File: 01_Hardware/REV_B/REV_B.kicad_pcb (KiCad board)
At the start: 2 copper layers, 65 x 30 mm, 65 parts, among them J1 RaspberryPi, J10 Conn_01x03, J11 Conn_01x03, J13 Conn_01x03, J14 Conn_01x03, J15 Conn_01x03, J16 Conn_01x08_Male, J2 Conn_01x02, J3 Conn_01x02, J4 Conn_01x02, J5 Conn_01x08_Male, J6 Conn_01x03, J7 Conn_01x03, J8 Conn_01x03, J9 Conn_01x03, U1 TB6612FNG, U2 MCP3008, U3 PCA9685PW, U5 BSS138PS, U6 BSS138PS, U7 BSS138PS, U8 BSS138PS

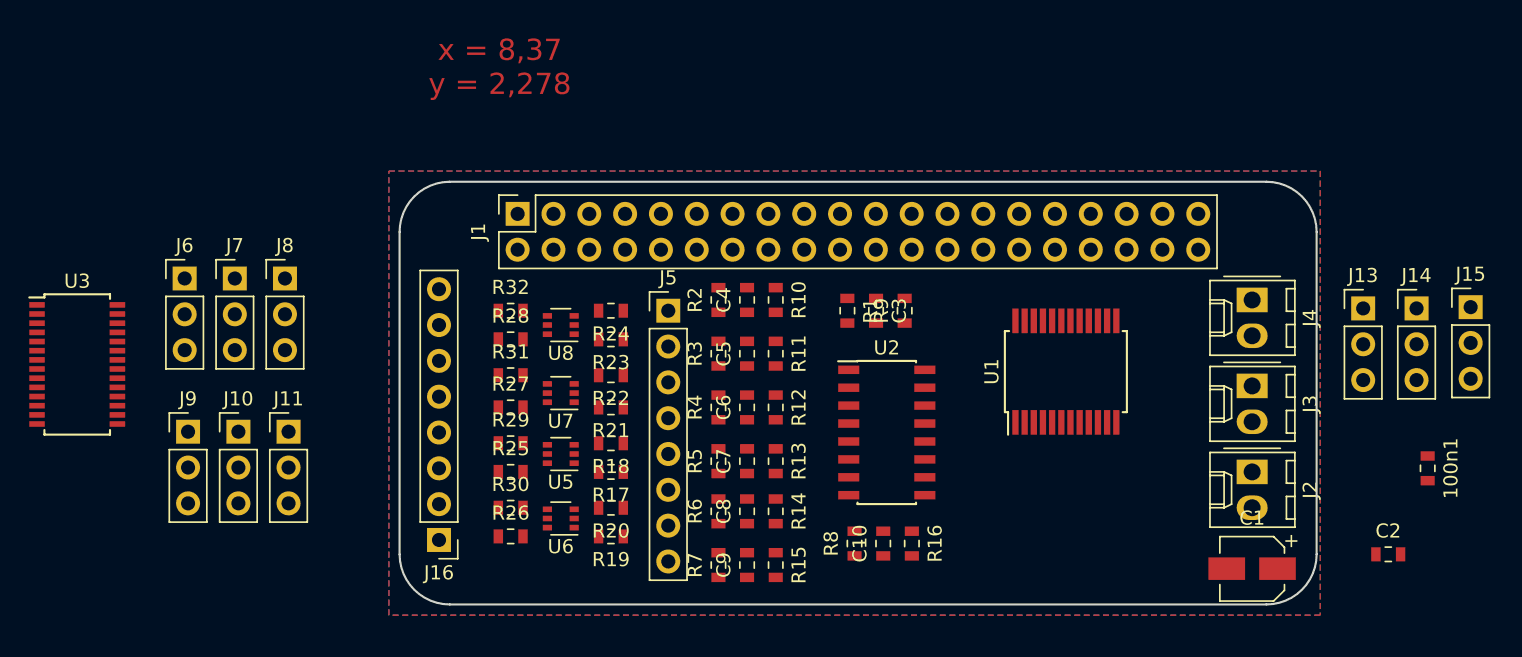
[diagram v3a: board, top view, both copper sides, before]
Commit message: kicad version  REVB added
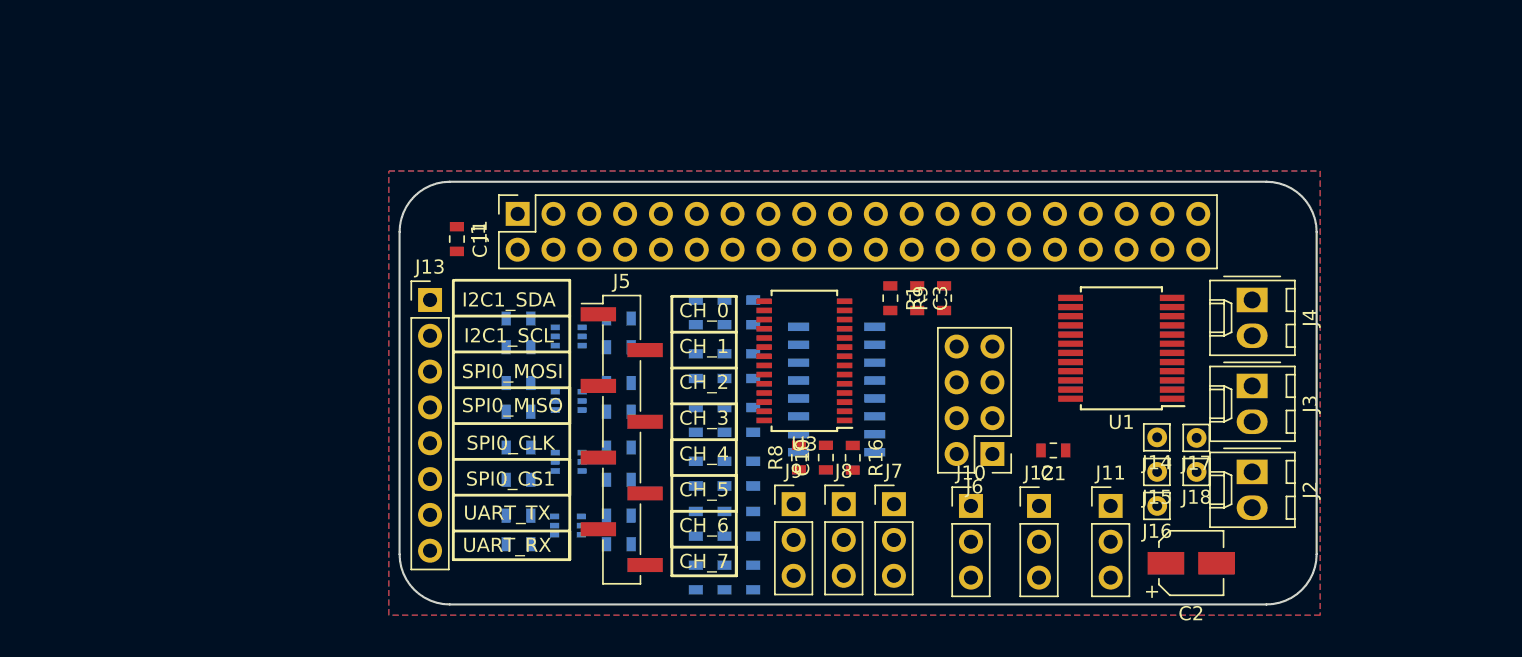
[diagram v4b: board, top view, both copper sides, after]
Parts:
- removed 100n1: C, Capacitor_SMD:C_0603_1608Metric
- removed U8: BSS138PS, Package_TO_SOT_SMD:SOT-363_SC-70-6
- added C11: 10n, Capacitor_SMD:C_0603_1608Metric, F.Cu at (4.06, 4.06)
- added J12: Conn_01x03, Connector_PinHeader_2.54mm:PinHeader_1x03_P2.54mm_Vertical, F.Cu at (45.3, 23.0)
- added J17: Conn_01x01, Connector_Pin:Pin_D0.7mm_L6.5mm_W1.8mm_FlatFork, F.Cu at (56.5, 18.2)
- added J18: Conn_01x01, Connector_Pin:Pin_D0.7mm_L6.5mm_W1.8mm_FlatFork, F.Cu at (56.5, 20.6)
- added U4: BSS138PS, Package_TO_SOT_SMD:SOT-363_SC-70-6, B.Cu at (11.9, 24.4)
- C1: value 10u -> 100n; footprint Capacitor_SMD:CP_Elec_4x4.5 -> Capacitor_SMD:C_0603_1608Metric
- C2: value 100n -> 10u; footprint Capacitor_SMD:C_0603_1608Metric -> Capacitor_SMD:CP_Elec_4x4.5
- C3: value 10n -> 100n
- C4, C5, C6, C7, C8, C9, R10, R11, R12, R13, R14, R15, R17, R18, R19, R2, R20, R21, R22, R23, R24, R25, R26, R27, R28, R29, R3, R30, R31, R32, R4, R5, R6, R7, U2, U5, U6, U7: moved to B.Cu
- J13: value Conn_01x03 -> Conn_01x08_Male; footprint Connector_PinHeader_2.54mm:PinHeader_1x03_P2.54mm_Vertical -> Connector_PinHeader_2.54mm:PinHeader_1x08_P2.54mm_Vertical
- J14, J15: value Conn_01x03 -> Conn_01x01; footprint Connector_PinHeader_2.54mm:PinHeader_1x03_P2.54mm_Vertical -> Connector_Pin:Pin_D0.7mm_L6.5mm_W1.8mm_FlatFork
- J16: value Conn_01x08_Male -> Conn_01x01; footprint Connector_PinHeader_2.54mm:PinHeader_1x08_P2.54mm_Vertical -> Connector_Pin:Pin_D0.7mm_L6.5mm_W1.8mm_FlatFork
- J5: footprint Connector_PinHeader_2.54mm:PinHeader_1x08_P2.54mm_Vertical -> Connector_PinHeader_2.54mm:PinHeader_1x08_P2.54mm_Vertical_SMD_Pin1Left
- J6: value Conn_01x03 -> Conn_02x04_Counter_Clockwise; footprint Connector_PinHeader_2.54mm:PinHeader_1x03_P2.54mm_Vertical -> Connector_PinHeader_2.54mm:PinHeader_2x04_P2.54mm_Vertical
- moved J13 66.2 mm to (2.16, 8.38)
- moved J6 58.6 mm to (42.0, 19.3), turned to 180 degrees
- moved J11 58.5 mm to (50.4, 23.0)
- moved J10 52.2 mm to (40.5, 23.0)
- moved U3 51.6 mm to (28.7, 12.7), turned to 180 degrees
- moved J16 51.0 mm to (53.7, 23.0), turned to 0 degrees
- moved J7 49.4 mm to (35.1, 22.9)
- moved J9 43.2 mm to (27.9, 22.9)
- moved J8 42.7 mm to (31.5, 22.9)
- moved J15 25.1 mm to (53.7, 20.6)
- moved J14 20.5 mm to (53.7, 18.1)
- moved R24 16.6 mm to (15.5, 25.7)
- moved R32 16.6 mm to (8.43, 25.7)
- moved C1 16.4 mm to (46.4, 19.1)
- moved R19 15.5 mm to (15.5, 9.70)
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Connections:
- C1 pad 1: +BATT -> +3V3
- C3 pad 1: Net-(C3-Pad1) -> +BATT
- J1 pad 10: (no net) -> UART_RX_LV
- J1 pad 19: Net-(J1-Pad19) -> SPI0_MOSI_LV
- J1 pad 21: Net-(J1-Pad21) -> SPI0_MISO_LV
- J1 pad 23: Net-(J1-Pad23) -> SPI0_CLK_LV
- J1 pad 26: (no net) -> SPI0_CS1_LV
- J1 pad 3: (no net) -> I2C1_SDA_LV
- J1 pad 38: (no net) -> Net-(J1-Pad38)
- J1 pad 5: (no net) -> I2C1_SCL_LV
- J1 pad 8: (no net) -> UART_TX_LV
- J10 pad 1: Net-(J10-Pad1) -> +5V
- J10 pad 3: GND -> +5V
- J11 pad 1: Net-(J11-Pad1) -> +3V3
- J11 pad 2: +5V -> +3V3
- J11 pad 3: GND -> +3V3
- J13 pad 1: +5V -> I2C1_SDA_HV
- J13 pad 2: +5V -> I2C1_SCL_HV
- J13 pad 3: +5V -> Net-(J13-Pad3)
- J14 pad 1: +3V3 -> Net-(J14-Pad1)
- J15 pad 1: GND -> Net-(J15-Pad1)
- J7 pad 2: Net-(J7-Pad2) -> +5V
- J7 pad 3: Net-(J7-Pad3) -> GND
- J8 pad 2: Net-(J8-Pad2) -> +5V
- J8 pad 3: Net-(J8-Pad3) -> GND
- R1 pad 1: Net-(C3-Pad1) -> Net-(C4-Pad1)
- R10 pad 2: Net-(C4-Pad1) -> Net-(C5-Pad1)
- R11 pad 2: Net-(C5-Pad1) -> Net-(C6-Pad1)
- R12 pad 2: Net-(C6-Pad1) -> Net-(C7-Pad1)
- R13 pad 2: Net-(C7-Pad1) -> Net-(C8-Pad1)
- R14 pad 2: Net-(C8-Pad1) -> Net-(C9-Pad1)
- R15 pad 2: Net-(C9-Pad1) -> Net-(C10-Pad1)
- R16 pad 2: Net-(C10-Pad1) -> Net-(C11-Pad1)
- R17 pad 2: Net-(R17-Pad2) -> SPI0_MOSI_LV
- R18 pad 2: Net-(R18-Pad2) -> SPI0_MISO_LV
- R19 pad 2: Net-(R19-Pad2) -> I2C1_SDA_LV
- R2 pad 1: Net-(C4-Pad1) -> Net-(C5-Pad1)
- R20 pad 2: Net-(R20-Pad2) -> I2C1_SCL_LV
- R21 pad 2: Net-(R21-Pad2) -> SPI0_CLK_LV
- R22 pad 2: Net-(R22-Pad2) -> SPI0_CS1_LV
- R23 pad 2: Net-(R23-Pad2) -> UART_TX_LV
- R24 pad 2: Net-(R24-Pad2) -> UART_RX_LV
- R25 pad 2: Net-(J16-Pad3) -> Net-(J13-Pad3)
- R26 pad 2: Net-(J16-Pad1) -> I2C1_SDA_HV
- R27 pad 2: Net-(J16-Pad5) -> Net-(J13-Pad5)
- R28 pad 2: Net-(J16-Pad7) -> Net-(J13-Pad7)
- R29 pad 2: Net-(J16-Pad4) -> Net-(J13-Pad4)
- R3 pad 1: Net-(C5-Pad1) -> Net-(C6-Pad1)
- R30 pad 2: Net-(J16-Pad2) -> I2C1_SCL_HV
- R31 pad 2: Net-(J16-Pad6) -> Net-(J13-Pad6)
- R32 pad 2: Net-(J16-Pad8) -> Net-(J13-Pad8)
- R4 pad 1: Net-(C6-Pad1) -> Net-(C7-Pad1)
- R5 pad 1: Net-(C7-Pad1) -> Net-(C8-Pad1)
- R6 pad 1: Net-(C8-Pad1) -> Net-(C9-Pad1)
- R7 pad 1: Net-(C9-Pad1) -> Net-(C10-Pad1)
- R8 pad 1: Net-(C10-Pad1) -> Net-(C11-Pad1)
- R9 pad 2: Net-(C3-Pad1) -> Net-(C4-Pad1)
- U1 pad 16: (no net) -> Net-(J1-Pad38)
- U2 pad 1: Net-(C3-Pad1) -> Net-(C4-Pad1)
- U2 pad 11: Net-(J1-Pad19) -> SPI0_MOSI_LV
- U2 pad 12: Net-(J1-Pad21) -> SPI0_MISO_LV
- U2 pad 13: Net-(J1-Pad23) -> SPI0_CLK_LV
- U2 pad 2: Net-(C4-Pad1) -> Net-(C5-Pad1)
- U2 pad 3: Net-(C5-Pad1) -> Net-(C6-Pad1)
- U2 pad 4: Net-(C6-Pad1) -> Net-(C7-Pad1)
- U2 pad 5: Net-(C7-Pad1) -> Net-(C8-Pad1)
- U2 pad 6: Net-(C8-Pad1) -> Net-(C9-Pad1)
- U2 pad 7: Net-(C9-Pad1) -> Net-(C10-Pad1)
- U2 pad 8: Net-(C10-Pad1) -> Net-(C11-Pad1)
- U3 pad 10: Net-(J7-Pad2) -> Net-(J6-Pad5)
- U3 pad 11: Net-(J7-Pad3) -> Net-(J6-Pad6)
- U3 pad 12: Net-(J8-Pad1) -> Net-(J6-Pad7)
- U3 pad 13: Net-(J8-Pad2) -> Net-(J6-Pad8)
- U3 pad 15: Net-(J8-Pad3) -> Net-(J9-Pad1)
- U3 pad 16: (no net) -> Net-(J8-Pad1)
- U3 pad 17: (no net) -> Net-(J7-Pad1)
- U3 pad 18: (no net) -> Net-(J18-Pad1)
- U3 pad 19: Net-(J9-Pad1) -> Net-(J17-Pad1)
- U3 pad 20: Net-(J10-Pad1) -> Net-(J16-Pad1)
- U3 pad 21: Net-(J11-Pad1) -> Net-(J15-Pad1)
- U3 pad 22: (no net) -> Net-(J14-Pad1)
- U3 pad 26: (no net) -> I2C1_SCL_HV
- U3 pad 27: (no net) -> I2C1_SDA_HV
- U3 pad 9: Net-(J7-Pad1) -> Net-(J6-Pad4)
- U5 pad 1: Net-(R17-Pad2) -> I2C1_SDA_LV
- U5 pad 3: Net-(J16-Pad4) -> I2C1_SCL_HV
- U5 pad 4: Net-(R18-Pad2) -> I2C1_SCL_LV
- U5 pad 6: Net-(J16-Pad3) -> I2C1_SDA_HV
- U6 pad 1: Net-(R19-Pad2) -> SPI0_CLK_LV
- U6 pad 3: Net-(J16-Pad2) -> Net-(J13-Pad6)
- U6 pad 4: Net-(R20-Pad2) -> SPI0_CS1_LV
- U6 pad 6: Net-(J16-Pad1) -> Net-(J13-Pad5)
- U7 pad 1: Net-(R21-Pad2) -> UART_TX_LV
- U7 pad 3: Net-(J16-Pad6) -> Net-(J13-Pad8)
- U7 pad 4: Net-(R22-Pad2) -> UART_RX_LV
- U7 pad 6: Net-(J16-Pad5) -> Net-(J13-Pad7)
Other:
- board text added: "CH_0"
- board text added: "CH_1"
- board text added: "CH_2"
- board text added: "CH_3"
- board text added: "CH_4"
- board text added: "CH_5"
- board text added: "CH_6"
- board text added: "CH_7"
- board text added: "I2C1_SCL"
- board text added: "I2C1_SDA"
- board text added: "SPI0_CLK"
- board text added: "SPI0_CS1"
- board text added: "SPI0_MISO"
- board text added: "SPI0_MOSI"
- board text added: "UART_RX"
- board text added: "UART_TX"
- board text removed: "x = 8,37 y = 2,278"

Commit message: Routing started
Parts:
- removed J14, J15, J16, J17, J18: Conn_01x01, Connector_Pin:Pin_D0.7mm_L6.5mm_W1.8mm_FlatFork
- added D1: LED_CRGB, LED_SMD:LED_Avago_PLCC4_3.2x2.8mm_CW, F.Cu at (61.0, 27.1)
- added R33: 10k, Resistor_SMD:R_0603_1608Metric, B.Cu at (6.48, 10.7)
- added R34: 10k, Resistor_SMD:R_0603_1608Metric, B.Cu at (13.7, 19.1)
- added R35: 10k, Resistor_SMD:R_0603_1608Metric, B.Cu at (6.73, 21.3)
- added R36: 10k, Resistor_SMD:R_0603_1608Metric, B.Cu at (13.7, 24.4)
- added R37: 10k, Resistor_SMD:R_0603_1608Metric, B.Cu at (6.60, 26.7)
- added R38: 10k, Resistor_SMD:R_0603_1608Metric, B.Cu at (6.73, 13.6)
- added R39: 10k, Resistor_SMD:R_0603_1608Metric, B.Cu at (6.48, 8.38)
- added R40: 10k, Resistor_SMD:R_0603_1608Metric, B.Cu at (6.73, 18.8)
- added R41: 10k, Resistor_SMD:R_0603_1608Metric, B.Cu at (6.73, 24.5)
- added R42: 10k, Resistor_SMD:R_0603_1608Metric, B.Cu at (13.7, 15.7)
- added R43: 10k, Resistor_SMD:R_0603_1608Metric, B.Cu at (13.7, 10.7)
- added R44: 10k, Resistor_SMD:R_0603_1608Metric, B.Cu at (13.7, 21.3)
- added R45: 10k, Resistor_SMD:R_0603_1608Metric, B.Cu at (13.7, 26.7)
- C10, R16: moved to B.Cu
- C4, R10, U2: moved to F.Cu
- J13, J5: value Conn_01x08_Male -> Conn_01x08
- R13: value 22k -> 1k
- R17: value 10k -> 22k; moved to F.Cu
- R18, R19, R20, R21, R22, R23, R24, R25, R26, R27, R28, R29: value 10k -> 220
- R9: value 1k -> 10k
- moved R18 37.5 mm to (20.2, -20.9)
- moved R19 37.5 mm to (20.2, -27.5)
- moved R20 37.5 mm to (20.2, -25.5)
- moved R22 37.5 mm to (20.2, -16.1)
- moved R23 37.5 mm to (20.2, -13.5)
- moved R24 37.5 mm to (20.2, -11.5)
- moved R25 37.5 mm to (13.1, -22.9)
- moved R26 37.5 mm to (13.1, -27.5)
- moved R27 37.5 mm to (13.1, -18.4)
- moved R28 37.5 mm to (13.1, -13.5)
- moved R29 37.5 mm to (13.1, -20.9)
- moved R21 28.5 mm to (44.1, 18.5), turned to 90 degrees
- moved C11 26.4 mm to (20.9, 24.4), turned to 0 degrees
- moved U3 25.1 mm to (42.0, -8.51)
- moved R32 18.1 mm to (13.7, 8.38), turned to 180 degrees
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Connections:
- R10 pad 1: Net-(J5-Pad2) -> Net-(J5-Pad1)
- R10 pad 2: Net-(C5-Pad1) -> Net-(C4-Pad1)
- R11 pad 1: Net-(J5-Pad3) -> Net-(J5-Pad2)
- R11 pad 2: Net-(C6-Pad1) -> Net-(C5-Pad1)
- R12 pad 1: Net-(J5-Pad4) -> Net-(J5-Pad3)
- R12 pad 2: Net-(C7-Pad1) -> Net-(C6-Pad1)
- R13 pad 1: Net-(J5-Pad5) -> Net-(J5-Pad4)
- R13 pad 2: Net-(C8-Pad1) -> Net-(C7-Pad1)
- R14 pad 1: Net-(J5-Pad6) -> Net-(J5-Pad5)
- R14 pad 2: Net-(C9-Pad1) -> Net-(C8-Pad1)
- R15 pad 1: Net-(J5-Pad7) -> Net-(J5-Pad6)
- R15 pad 2: Net-(C10-Pad1) -> Net-(C9-Pad1)
- R16 pad 1: Net-(J5-Pad8) -> Net-(J5-Pad7)
- R16 pad 2: Net-(C11-Pad1) -> Net-(C10-Pad1)
- R17 pad 1: +3V3 -> Net-(J5-Pad8)
- R17 pad 2: SPI0_MOSI_LV -> Net-(C11-Pad1)
- R18 pad 1: +3V3 -> Net-(D1-Pad2)
- R18 pad 2: SPI0_MISO_LV -> Net-(R18-Pad2)
- R19 pad 1: +3V3 -> Net-(D1-Pad3)
- R19 pad 2: I2C1_SDA_LV -> Net-(R19-Pad2)
- R20 pad 1: +3V3 -> Net-(D1-Pad4)
- R20 pad 2: I2C1_SCL_LV -> Net-(R20-Pad2)
- R21 pad 1: +3V3 -> Net-(J6-Pad1)
- R21 pad 2: SPI0_CLK_LV -> Net-(R21-Pad2)
- R22 pad 1: +3V3 -> Net-(J6-Pad2)
- R22 pad 2: SPI0_CS1_LV -> Net-(R22-Pad2)
- R23 pad 1: +3V3 -> Net-(J6-Pad3)
- R23 pad 2: UART_TX_LV -> Net-(R23-Pad2)
- R24 pad 1: +3V3 -> Net-(J6-Pad4)
- R24 pad 2: UART_RX_LV -> Net-(R24-Pad2)
- R25 pad 1: +5V -> Net-(J6-Pad5)
- R25 pad 2: Net-(J13-Pad3) -> Net-(R25-Pad2)
- R26 pad 1: +5V -> Net-(J6-Pad6)
- R26 pad 2: I2C1_SDA_HV -> Net-(R26-Pad2)
- R27 pad 1: +5V -> Net-(J6-Pad7)
- R27 pad 2: Net-(J13-Pad5) -> Net-(R27-Pad2)
- R28 pad 1: +5V -> Net-(J6-Pad8)
- R28 pad 2: Net-(J13-Pad7) -> Net-(R28-Pad2)
- R29 pad 1: +5V -> Net-(J9-Pad1)
- R29 pad 2: Net-(J13-Pad4) -> Net-(R29-Pad2)
- R30 pad 1: +5V -> +3V3
- R30 pad 2: I2C1_SCL_HV -> SPI0_MOSI_LV
- R31 pad 1: +5V -> +3V3
- R31 pad 2: Net-(J13-Pad6) -> SPI0_MISO_LV
- R32 pad 1: +5V -> +3V3
- R32 pad 2: Net-(J13-Pad8) -> I2C1_SDA_LV
- R9 pad 1: Net-(J5-Pad1) -> GND
- R9 pad 2: Net-(C4-Pad1) -> Net-(R9-Pad2)
- U3 pad 10: Net-(J6-Pad5) -> Net-(R25-Pad2)
- U3 pad 11: Net-(J6-Pad6) -> Net-(R26-Pad2)
- U3 pad 12: Net-(J6-Pad7) -> Net-(R27-Pad2)
- U3 pad 13: Net-(J6-Pad8) -> Net-(R28-Pad2)
- U3 pad 15: Net-(J9-Pad1) -> Net-(R29-Pad2)
- U3 pad 18: Net-(J18-Pad1) -> Net-(R20-Pad2)
- U3 pad 19: Net-(J17-Pad1) -> Net-(R19-Pad2)
- U3 pad 20: Net-(J16-Pad1) -> Net-(R18-Pad2)
- U3 pad 21: Net-(J15-Pad1) -> (no net)
- U3 pad 22: Net-(J14-Pad1) -> (no net)
- U3 pad 23: (no net) -> Net-(R9-Pad2)
- U3 pad 6: Net-(J6-Pad1) -> Net-(R21-Pad2)
- U3 pad 7: Net-(J6-Pad2) -> Net-(R22-Pad2)
- U3 pad 8: Net-(J6-Pad3) -> Net-(R23-Pad2)
- U3 pad 9: Net-(J6-Pad4) -> Net-(R24-Pad2)
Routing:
- net +5V: track 0.00 -> 84.8 mm, vias 0 -> 2
- net +3V3: track 0.00 -> 75.4 mm, vias 0 -> 5
- net SPI0_CLK_LV: track 0.00 -> 48.3 mm, vias 0 -> 1
- net SPI0_CS1_LV: track 0.00 -> 45.8 mm, vias 0 -> 1
- net UART_TX_LV: track 0.00 -> 44.9 mm, vias 0 -> 1
- net UART_RX_LV: track 0.00 -> 39.1 mm, vias 0 -> 2
- net Net-(J1-Pad24): track 0.00 -> 21.6 mm
- net SPI0_MISO_LV: track 0.00 -> 21.5 mm
- net SPI0_MOSI_LV: track 0.00 -> 20.6 mm, vias 0 -> 1
- net I2C1_SDA_LV: track 0.00 -> 16.1 mm, vias 0 -> 1
- net Net-(J5-Pad1): track 0.00 -> 15.7 mm
- net Net-(J13-Pad8): track 0.00 -> 14.2 mm
- net I2C1_SCL_LV: track 0.00 -> 13.8 mm, vias 0 -> 1
- net Net-(J13-Pad6): track 0.00 -> 12.4 mm
- net Net-(J13-Pad4): track 0.00 -> 12.3 mm
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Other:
- net class Default: clearance 0.2 -> 0.1524; trace_width 0.25 -> 0.1524; via_dia 0.8 -> 0.6858; via_drill 0.4 -> 0.3302
- rule pad_to_mask_clearance: 0.2 -> 0.0508
- rule trace_clearance: 0.2 -> 0.1524
- rule trace_min: 0.2 -> 0.1524
- rule via_min_drill: 0.3 -> 0.254
- rule via_min_size: 0.4 -> 0.508

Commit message: Routing almost done
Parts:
- C3, U1, U3: moved to B.Cu
- J6: footprint Connector_PinHeader_2.54mm:PinHeader_2x04_P2.54mm_Vertical -> Connector_PinHeader_2.54mm:PinHeader_2x04_P2.54mm_Vertical_SMD
- moved R26 49.0 mm to (36.2, 15.7), turned to 180 degrees
- moved R19 48.3 mm to (27.6, 20.2)
- moved R20 46.9 mm to (31.1, 20.2), turned to 0 degrees
- moved R29 45.1 mm to (24.5, 22.7), turned to 90 degrees
- moved R25 43.5 mm to (36.2, 14.0), turned to 180 degrees
- moved R27 42.7 mm to (36.2, 17.5), turned to 180 degrees
- moved R28 40.1 mm to (36.2, 19.3), turned to 180 degrees
- moved R18 36.8 mm to (24.6, 15.6), turned to 90 degrees
- moved R22 29.4 mm to (36.2, 8.64)
- moved R23 28.8 mm to (36.2, 10.4)
- moved R24 28.6 mm to (36.2, 12.2)
- moved U3 25.4 mm to (29.7, 13.7)
- moved C3 16.7 mm to (57.5, 9.65)
- moved R21 14.1 mm to (36.2, 6.86), turned to 180 degrees
- moved J6 7.37 mm to (35.3, 13.2), turned to 0 degrees
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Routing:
- net Net-(R21-Pad2): track 0.00 -> 11.1 mm
- net Net-(J6-Pad1): track 0.00 -> 7.40 mm, vias 0 -> 1
- net Net-(R22-Pad2): track 0.00 -> 6.81 mm
- net Net-(J6-Pad5): track 0.00 -> 5.44 mm, vias 0 -> 1
- net Net-(R23-Pad2): track 0.00 -> 5.31 mm
- net Net-(J6-Pad7): track 0.00 -> 5.26 mm, vias 0 -> 1
- net Net-(J6-Pad3): track 0.00 -> 4.92 mm, vias 0 -> 1
- net Net-(R28-Pad2): track 0.00 -> 4.15 mm
- net Net-(R24-Pad2): track 0.00 -> 4.02 mm
- net Net-(J6-Pad2): track 0.00 -> 3.83 mm, vias 0 -> 1
- net Net-(R25-Pad2): track 0.00 -> 3.32 mm
- net Net-(R27-Pad2): track 0.00 -> 3.22 mm
- net Net-(J6-Pad8): track 0.00 -> 3.16 mm, vias 0 -> 1
- net Net-(J6-Pad4): track 0.00 -> 3.01 mm, vias 0 -> 1
- net Net-(R26-Pad2): track 0.00 -> 2.98 mm
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
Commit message: Reorder
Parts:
- added R46: 220, Resistor_SMD:R_0603_1608Metric, B.Cu at (29.6, 25.9)
- added R47: 220, Resistor_SMD:R_0603_1608Metric, B.Cu at (29.6, 24.1)
- C11, C4, R1, R10, R17, R8, R9, U2: moved to B.Cu
- U1: moved to F.Cu
- moved R18 31.9 mm to (53.8, 28.3), turned to 180 degrees
- moved R19 27.0 mm to (53.8, 26.5)
- moved R20 23.2 mm to (53.8, 24.8), turned to 180 degrees
- moved J5 11.6 mm to (24.1, 18.0)
- moved R21 7.71 mm to (43.8, 8.00)
- moved R22 7.71 mm to (43.8, 9.78)
- moved R23 7.71 mm to (43.8, 11.6)
- moved R24 7.71 mm to (43.8, 13.3)
- moved R25 7.71 mm to (43.8, 15.1)
- moved R26 7.71 mm to (43.8, 16.9)
- moved R27 7.71 mm to (43.8, 18.7)
- moved R28 7.71 mm to (43.8, 20.4)
- moved U3 7.58 mm to (37.1, 15.5)
- moved R29 7.09 mm to (29.6, 27.7), turned to 180 degrees
- moved R1 7.00 mm to (28.3, 8.26), turned to 90 degrees
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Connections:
- U3 pad 16: Net-(J8-Pad1) -> Net-(R46-Pad2)
- U3 pad 17: Net-(J7-Pad1) -> Net-(R47-Pad2)
- U3 pad 18: Net-(R20-Pad2) -> (no net)
- U3 pad 19: Net-(R19-Pad2) -> (no net)
- U3 pad 20: Net-(R18-Pad2) -> Net-(R20-Pad2)
- U3 pad 21: (no net) -> Net-(R19-Pad2)
- U3 pad 22: (no net) -> Net-(R18-Pad2)
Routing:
- net +5V: track 84.8 -> 0.00 mm, vias 2 -> 0
- net +3V3: track 75.4 -> 0.00 mm, vias 5 -> 0
- net SPI0_CLK_LV: track 48.3 -> 0.00 mm, vias 1 -> 0
- net SPI0_CS1_LV: track 45.8 -> 0.00 mm, vias 1 -> 0
- net UART_TX_LV: track 44.9 -> 0.00 mm, vias 1 -> 0
- net UART_RX_LV: track 39.1 -> 0.00 mm, vias 2 -> 0
- net Net-(J1-Pad24): track 21.6 -> 0.00 mm
- net SPI0_MISO_LV: track 21.5 -> 0.00 mm
- net SPI0_MOSI_LV: track 20.6 -> 0.00 mm, vias 1 -> 0
- net I2C1_SDA_LV: track 16.1 -> 0.00 mm, vias 1 -> 0
- net Net-(J5-Pad1): track 15.7 -> 0.00 mm
- net Net-(J13-Pad8): track 14.2 -> 0.00 mm
- net I2C1_SCL_LV: track 13.8 -> 0.00 mm, vias 1 -> 0
- net Net-(J13-Pad6): track 12.4 -> 0.00 mm
- net Net-(J13-Pad4): track 12.3 -> 0.00 mm
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
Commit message: remaning resistors added to PCA9685 w/ routing
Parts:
- moved J5 8.90 mm to (15.2, 17.5)
- moved U7 0.36 mm to (10.3, 25.7)
- moved R37 0.28 mm to (6.73, 26.9)
- moved R33 0.18 mm to (6.60, 10.8)
- moved R39 0.13 mm to (6.60, 8.38), turned to 180 degrees
- turned R38 to 180 degrees
- turned R40 to 180 degrees
- turned R41 to 180 degrees
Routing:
- net +3V3: track 0.00 -> 71.9 mm, vias 0 -> 4
- net +5V: track 0.00 -> 58.2 mm, vias 0 -> 4
- net UART_RX_LV: track 0.00 -> 32.1 mm, vias 0 -> 1
- net UART_TX_LV: track 0.00 -> 25.8 mm, vias 0 -> 1
- net I2C1_SCL_LV: track 0.00 -> 13.4 mm, vias 0 -> 1
- net Net-(J13-Pad8): track 0.00 -> 13.2 mm
- net Net-(J13-Pad6): track 0.00 -> 12.4 mm
- net I2C1_SCL_HV: track 0.00 -> 12.2 mm
- net Net-(J13-Pad4): track 0.00 -> 12.0 mm
- net I2C1_SDA_LV: track 0.00 -> 8.95 mm
- net Net-(J13-Pad7): track 0.00 -> 8.06 mm
- net Net-(J13-Pad5): track 0.00 -> 7.67 mm
- net Net-(J13-Pad3): track 0.00 -> 7.62 mm
- net I2C1_SDA_HV: track 0.00 -> 7.45 mm
- net Net-(C5-Pad1): track 0.00 -> 4.15 mm
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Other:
- board text added: "Analog"
